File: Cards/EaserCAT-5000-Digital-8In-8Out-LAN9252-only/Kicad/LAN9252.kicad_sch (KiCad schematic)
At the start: 16 parts, among them U3 LAN9252_PT, Y1 25MHz

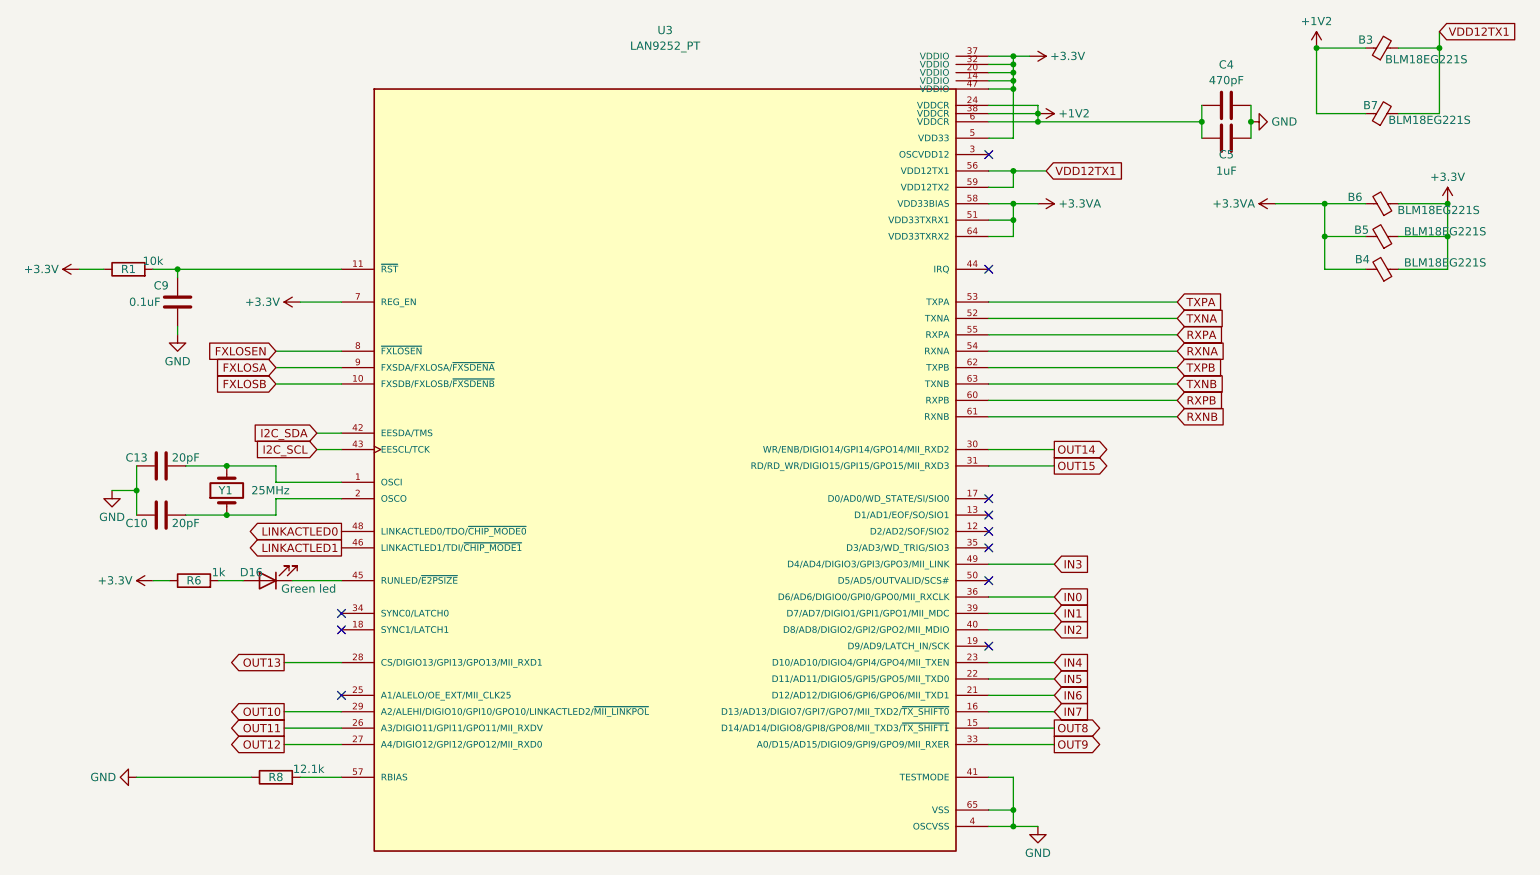
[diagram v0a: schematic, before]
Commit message: Updated 24V field voltage routing. Files sent for fab
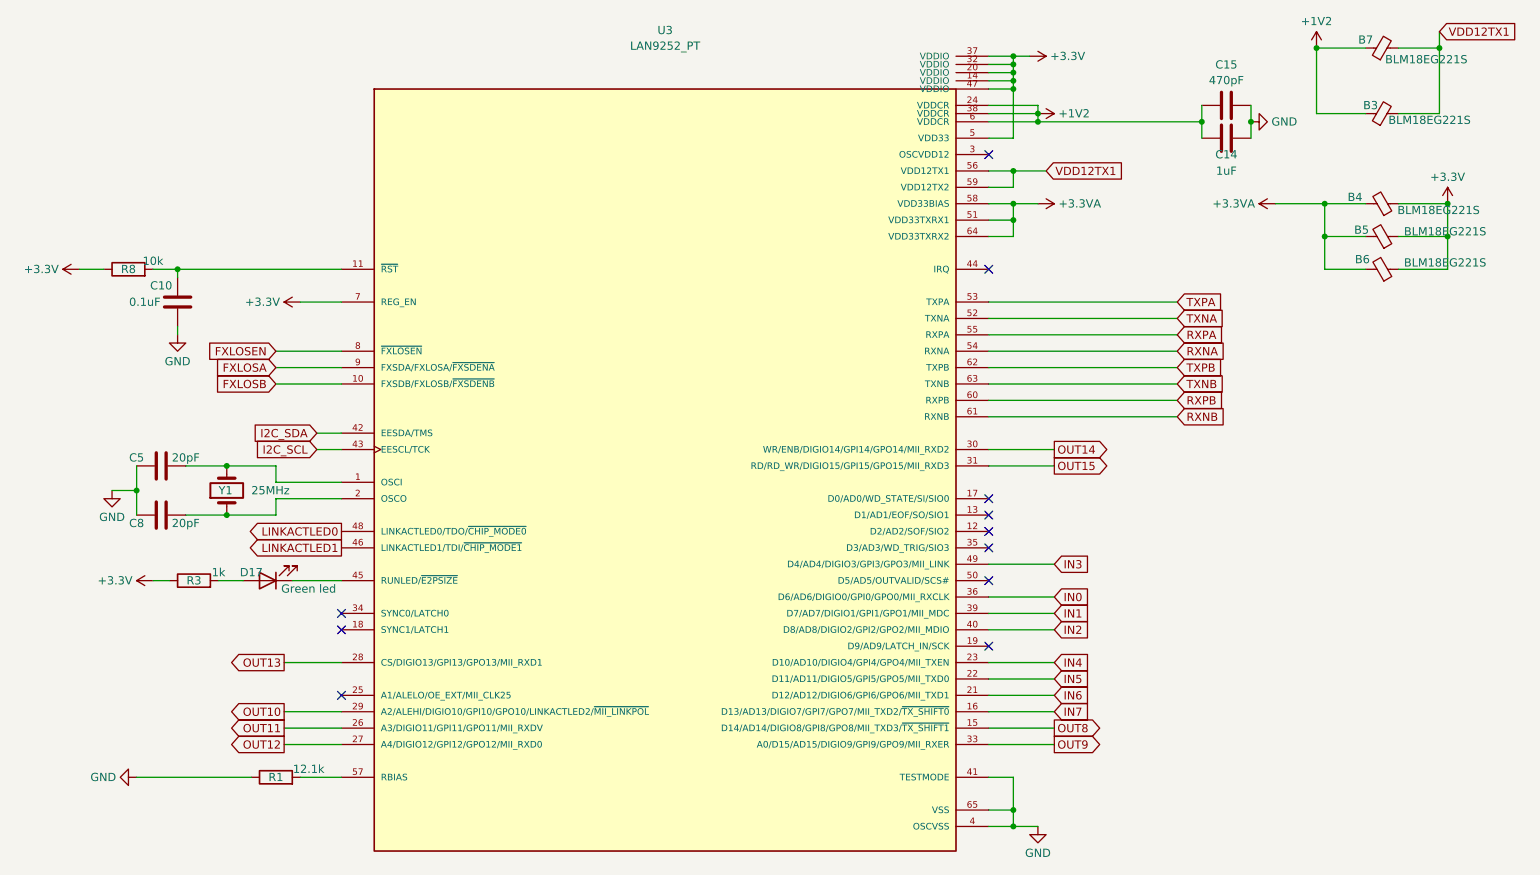
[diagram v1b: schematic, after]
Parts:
- renumbered B7 to B3, B6 to B4, B4 to B6, B3 to B7, C9 to C10, C5 to C14, C4 to C15, C13 to C5, C10 to C8, D16 to D17, R8 to R1, R6 to R3, R1 to R8
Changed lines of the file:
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@@
 		(on_board yes)
 		(dnp no)
-		(property "Reference" "R6"
+		(property "Reference" "R3"
 			(at 76.2 107.95 90)
 			(effects
@@
 			(project "THCAD-reader"
 				(path "/5597aedc-b607-407f-bbfd-31b3b298ecb1/a120273a-c1ae-42b3-935d-01f789f654a3"
-					(reference "R6")
+					(reference "R3")
 					(unit 1)
 				)
@@
 		(on_board yes)
 		(dnp no)
-		(property "Reference" "B7"
+		(property "Reference" "B3"
 			(at 258.572 34.29 90)
 			(effects
@@
 			(project "8In-8Out-LAN9252-only"
 				(path "/5597aedc-b607-407f-bbfd-31b3b298ecb1/a120273a-c1ae-42b3-935d-01f789f654a3"
-					(reference "B7")
+					(reference "B3")
 					(unit 1)
 				)
@@
 		(on_board yes)
 		(dnp no)
-		(property "Reference" "B3"
+		(property "Reference" "B7"
 			(at 257.81 24.13 90)
 			(effects
@@
 			(project "8In-8Out-LAN9252-only"
 				(path "/5597aedc-b607-407f-bbfd-31b3b298ecb1/a120273a-c1ae-42b3-935d-01f789f654a3"
-					(reference "B3")
+					(reference "B7")
 					(unit 1)
 				)
@@
 		(on_board yes)
 		(dnp no)
-		(property "Reference" "R8"
+		(property "Reference" "R1"
 			(at 88.9 138.43 90)
 			(effects
@@
 			(project "THCAD-reader"
 				(path "/5597aedc-b607-407f-bbfd-31b3b298ecb1/a120273a-c1ae-42b3-935d-01f789f654a3"
-					(reference "R8")
+					(reference "R1")
 					(unit 1)
 				)
@@
 		(on_board yes)
 		(dnp no)
-		(property "Reference" "D16"
+		(property "Reference" "D17"
 			(at 85.09 106.68 0)
 			(effects
@@
 			(project "THCAD-reader"
 				(path "/5597aedc-b607-407f-bbfd-31b3b298ecb1/a120273a-c1ae-42b3-935d-01f789f654a3"
-					(reference "D16")
+					(reference "D17")
 					(unit 1)
 				)
@@
 		(on_board yes)
 		(dnp no)
-		(property "Reference" "C10"
+		(property "Reference" "C8"
 			(at 67.31 99.06 90)
 			(effects
@@
 			(project "THCAD-reader"
 				(path "/5597aedc-b607-407f-bbfd-31b3b298ecb1/a120273a-c1ae-42b3-935d-01f789f654a3"
-					(reference "C10")
+					(reference "C8")
 					(unit 1)
 				)
@@
 		(on_board yes)
 		(dnp no)
-		(property "Reference" "B4"
+		(property "Reference" "B6"
 			(at 257.302 58.166 90)
 			(effects
@@
 			(project "8In-8Out-LAN9252-only"
 				(path "/5597aedc-b607-407f-bbfd-31b3b298ecb1/a120273a-c1ae-42b3-935d-01f789f654a3"
-					(reference "B4")
+					(reference "B6")
 					(unit 1)
 				)
@@
 		(dnp no)
 		(fields_autoplaced yes)
-		(property "Reference" "C4"
+		(property "Reference" "C15"
 			(at 236.22 27.9867 90)
 			(effects
@@
 			(project "THCAD-reader"
 				(path "/5597aedc-b607-407f-bbfd-31b3b298ecb1/a120273a-c1ae-42b3-935d-01f789f654a3"
-					(reference "C4")
+					(reference "C15")
 					(unit 1)
 				)
@@
 		(on_board yes)
 		(dnp no)
-		(property "Reference" "C5"
+		(property "Reference" "C14"
 			(at 236.22 41.91 90)
 			(effects
@@
 			(project "THCAD-reader"
 				(path "/5597aedc-b607-407f-bbfd-31b3b298ecb1/a120273a-c1ae-42b3-935d-01f789f654a3"
-					(reference "C5")
+					(reference "C14")
 					(unit 1)
 				)
@@
 		(on_board yes)
 		(dnp no)
-		(property "Reference" "C9"
+		(property "Reference" "C10"
 			(at 71.12 62.23 0)
 			(effects
@@
 			(project "THCAD-reader"
 				(path "/5597aedc-b607-407f-bbfd-31b3b298ecb1/a120273a-c1ae-42b3-935d-01f789f654a3"
-					(reference "C9")
+					(reference "C10")
 					(unit 1)
 				)
@@
 		(on_board yes)
 		(dnp no)
-		(property "Reference" "R1"
+		(property "Reference" "R8"
 			(at 66.04 59.69 90)
 			(effects
@@
 			(project "THCAD-reader"
 				(path "/5597aedc-b607-407f-bbfd-31b3b298ecb1/a120273a-c1ae-42b3-935d-01f789f654a3"
-					(reference "R1")
+					(reference "R8")
 					(unit 1)
 				)
@@
 		(on_board yes)
 		(dnp no)
-		(property "Reference" "C13"
+		(property "Reference" "C5"
 			(at 67.31 88.9 90)
 			(effects
@@
 			(project "THCAD-reader"
 				(path "/5597aedc-b607-407f-bbfd-31b3b298ecb1/a120273a-c1ae-42b3-935d-01f789f654a3"
-					(reference "C13")
+					(reference "C5")
 					(unit 1)
 				)
@@
 		(on_board yes)
 		(dnp no)
-		(property "Reference" "B6"
+		(property "Reference" "B4"
 			(at 256.159 48.514 90)
 			(effects
@@
 			(project "8In-8Out-LAN9252-only"
 				(path "/5597aedc-b607-407f-bbfd-31b3b298ecb1/a120273a-c1ae-42b3-935d-01f789f654a3"
-					(reference "B6")
-					(unit 1)
-				)
+					(reference "B4")
+					(unit 1)
+				)

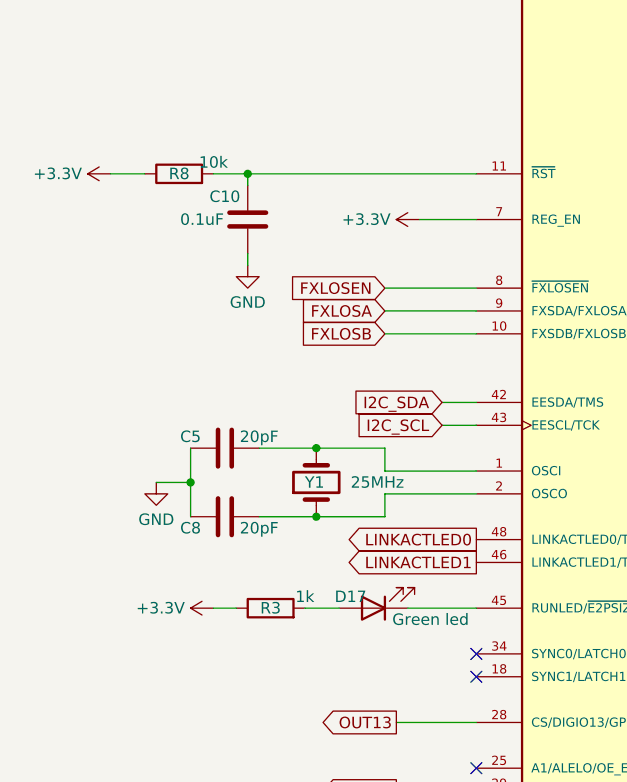
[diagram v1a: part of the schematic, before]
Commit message: Updates to hw straps after startup of card.
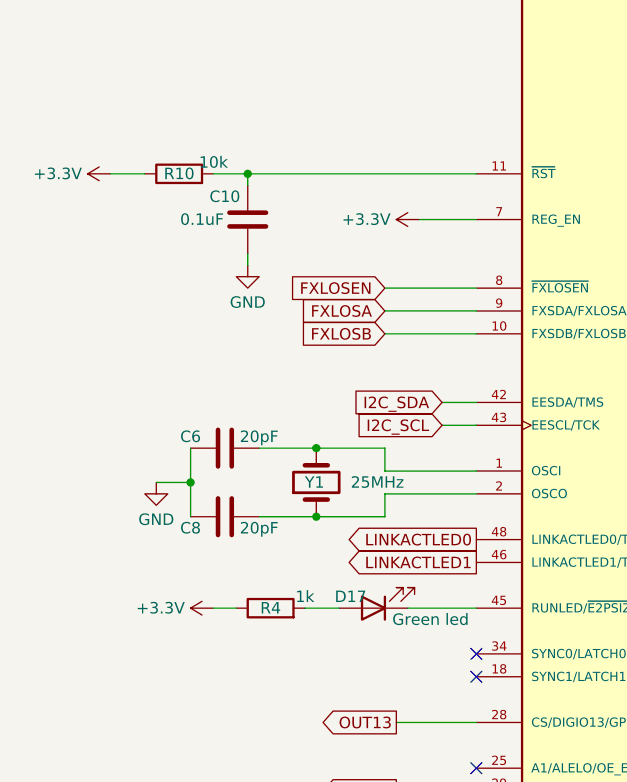
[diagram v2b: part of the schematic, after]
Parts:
- renumbered C5 to C6, R8 to R10, R3 to R4
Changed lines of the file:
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@@
 		(on_board yes)
 		(dnp no)
-		(property "Reference" "R3"
+		(property "Reference" "R4"
 			(at 76.2 107.95 90)
 			(effects
@@
 			(project "THCAD-reader"
 				(path "/5597aedc-b607-407f-bbfd-31b3b298ecb1/a120273a-c1ae-42b3-935d-01f789f654a3"
-					(reference "R3")
+					(reference "R4")
 					(unit 1)
 				)
@@
 		(on_board yes)
 		(dnp no)
-		(property "Reference" "R8"
+		(property "Reference" "R10"
 			(at 66.04 59.69 90)
 			(effects
@@
 			(project "THCAD-reader"
 				(path "/5597aedc-b607-407f-bbfd-31b3b298ecb1/a120273a-c1ae-42b3-935d-01f789f654a3"
-					(reference "R8")
+					(reference "R10")
 					(unit 1)
 				)
@@
 		(on_board yes)
 		(dnp no)
-		(property "Reference" "C5"
+		(property "Reference" "C6"
 			(at 67.31 88.9 90)
 			(effects
@@
 			(project "THCAD-reader"
 				(path "/5597aedc-b607-407f-bbfd-31b3b298ecb1/a120273a-c1ae-42b3-935d-01f789f654a3"
-					(reference "C5")
-					(unit 1)
-				)
+					(reference "C6")
+					(unit 1)
+				)
